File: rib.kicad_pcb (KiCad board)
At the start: 2 copper layers, 140 x 90 mm, 94 parts, among them J1 RJ45_LED, J10 Conn_01x04_Male, J11 Screw_Terminal_01x02, J12 Screw_Terminal_01x02, J13 Screw_Terminal_01x02, J14 Conn_01x02_Male, J15 Conn_01x02_Male, J16 Conn_01x06_Male, J2 RJ45_LED, J3 RJ45_LED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

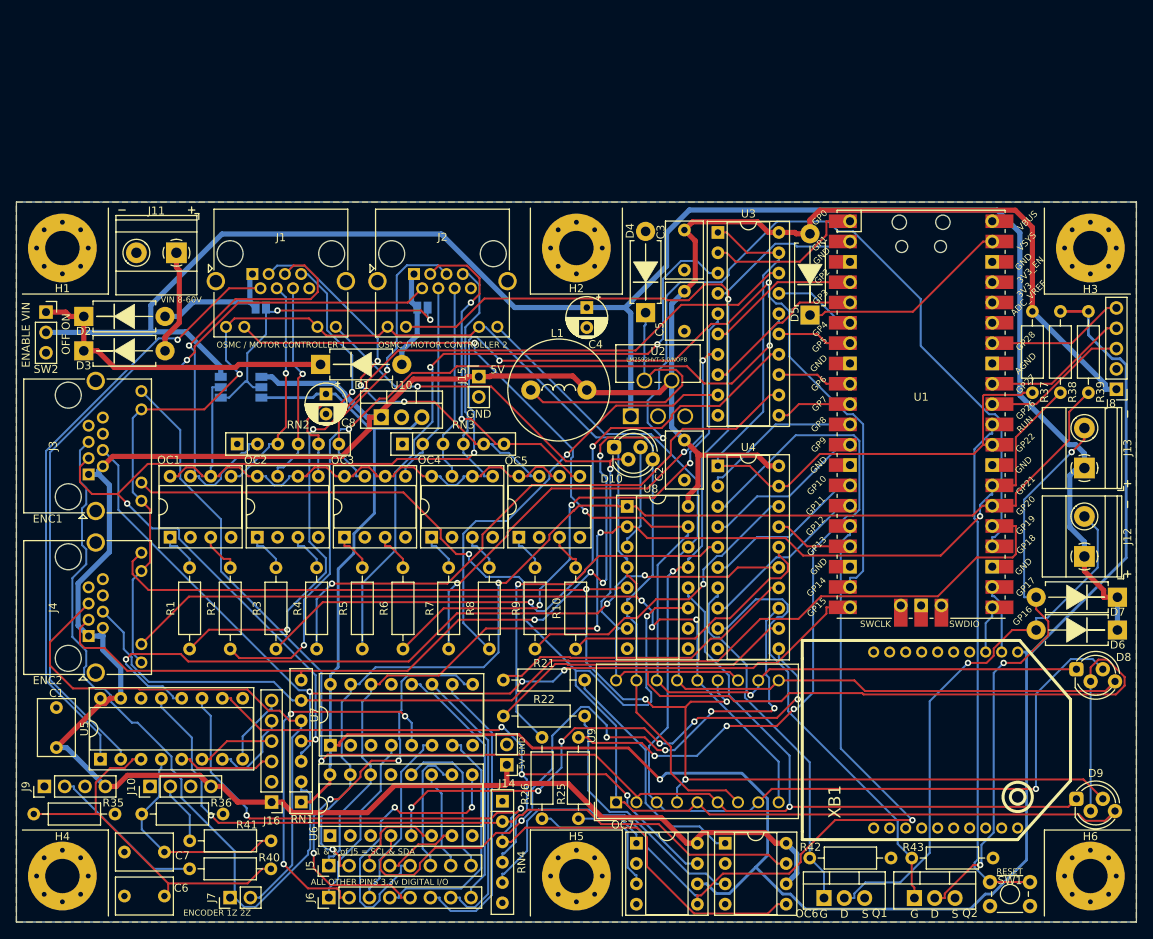
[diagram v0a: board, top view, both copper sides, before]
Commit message: Fix via stitching
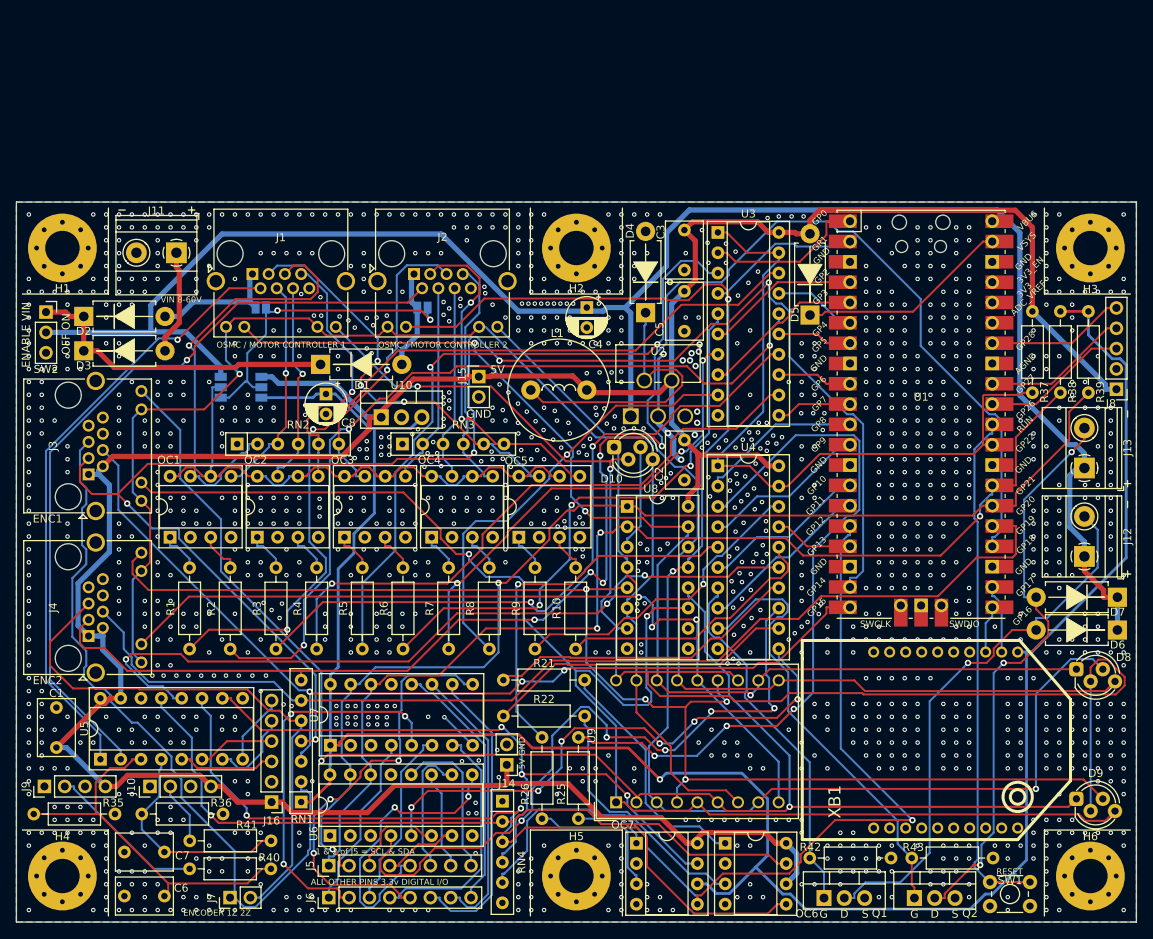
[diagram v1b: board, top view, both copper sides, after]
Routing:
- net GND: track 0.00 -> 19.8 mm, vias 0 -> 1422
- net Net-(RN1-R6): track 198.8 -> 200.0 mm
- net Net-(J5-Pin_5): track 37.6 -> 36.7 mm
- net LED8: track 122.2 -> 122.7 mm

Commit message: prepare to add zener diode
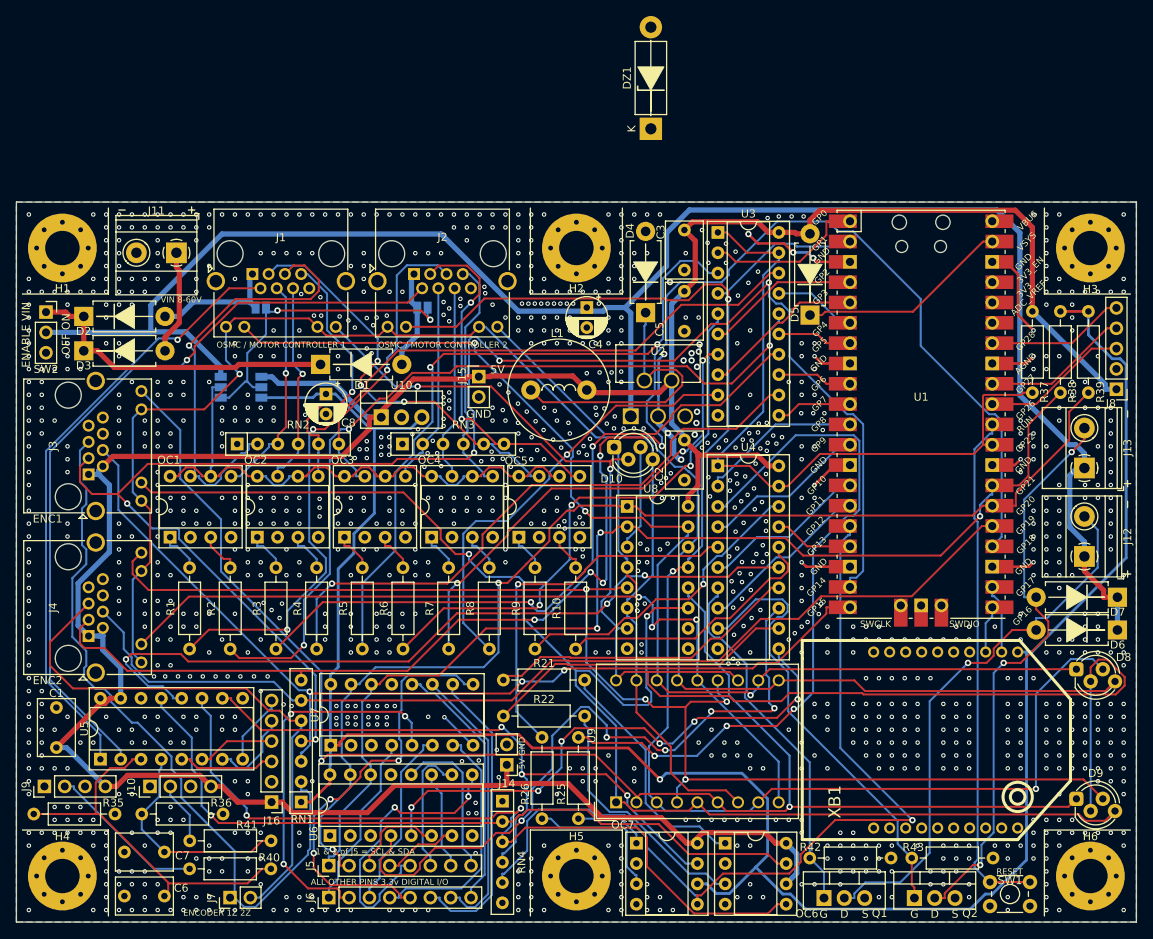
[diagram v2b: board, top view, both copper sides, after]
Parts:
- added DZ1: 1N5339B, Diode_THT_AKL:D_5W_CASE-017AA_P12.70mm_Horizontal_Zener, F.Cu at (114.8, 37.8)
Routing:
- net GND: track 19.8 -> 77.1 mm, vias 1422 -> 1221
- net Net-(RN1-R5): track 134.6 -> 126.7 mm

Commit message: v1.0 design update (BOMs not updated)
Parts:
- moved DZ1 24.9 mm to (114.1, 62.8)
- moved C4 16.5 mm to (93.7, 70.3)
- moved J15 6.06 mm to (87.5, 67.2), turned to 90 degrees
- moved D4 3.87 mm to (110.3, 60.9), turned to 180 degrees
- moved D10 0.14 mm to (110.2, 77.8)
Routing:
- net 5V: track 376.8 -> 479.7 mm, vias 0 -> 1
- net Net-(RN1-R2): track 123.4 -> 199.5 mm, vias 3 -> 7
- net GND: track 77.1 -> 2.54 mm, vias 1221 -> 2419
- net SDA: track 145.1 -> 215.3 mm, vias 2 -> 4
- net Net-(U1-GPIO16): track 5.93 -> 73.1 mm, vias 0 -> 5
- net Net-(J6-Pin_6): track 37.8 -> 92.1 mm, vias 0 -> 3
- net SCL: track 142.4 -> 190.8 mm, vias 3 -> 4
- net Net-(RN1-R3): track 202.4 -> 154.8 mm, vias 5 -> 3
- net Net-(RN3-R4): track 51.9 -> 97.4 mm, vias 3 -> 0
- net Net-(J6-Pin_7): track 35.1 -> 79.4 mm, vias 0 -> 3
- net Net-(U1-GPIO22): track 88.5 -> 126.2 mm
- net Net-(U3-1Y3): track 76.7 -> 113.7 mm
- net Net-(U4-2Y0): track 89.7 -> 59.9 mm, vias 3 -> 1
- net Net-(RN4-R4): track 110.8 -> 139.1 mm, vias 1 -> 5
- net Net-(U3-1Y2): track 88.1 -> 115.4 mm, vias 2 -> 1
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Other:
- board text added: "Designed by Amelia Deck for ILLINOIS TECH ROBOTICS Robot Interface Board (RIB) V1.0 inspired by GOLIATH design by Nash Kaminski with help from Scarlett Kadan Iliyan Jivraj"
- board text removed: "Designed by Amelia Deck for ILLINOIS TECH ROBOTICS Robot Interface Board (RIB) V1.0-RC1 inspired by GOLIATH design by Nash Kaminski with help from Scarlett Kadan Iliyan Jivraj"

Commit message: RIB v1.1 pre-release, documentation
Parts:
- removed R35, R36: 10k, Resistor_THT:R_Axial_DIN0207_L6.3mm_D2.5mm_P10.16mm_Horizontal
- added J17: Conn_01x02_Male, Connector_PinHeader_2.54mm:PinHeader_1x02_P2.54mm_Vertical, F.Cu at (65.5, 126.8)
- added J18: Conn_01x02_Male, Connector_PinHeader_2.54mm:PinHeader_1x02_P2.54mm_Vertical, F.Cu at (60.9, 126.7)
- added J19: Conn_01x02_Male, Connector_PinHeader_2.54mm:PinHeader_1x02_P2.54mm_Vertical, F.Cu at (54.6, 70.4)
- C6, C7: value 1uF -> 10uF
- J7: value Conn_01x02_Male -> Conn_01x04_Male; footprint Connector_PinHeader_2.54mm:PinHeader_1x02_P2.54mm_Vertical -> Connector_PinHeader_2.54mm:PinHeader_1x04_P2.54mm_Vertical
- R40, R41: value 33k -> 10k
- RN1: value 10k_Network06 -> R_Network08; footprint Resistor_THT:R_Array_SIP7 -> Resistor_THT:R_Array_SIP9
- moved R40 20.5 mm to (37.8, 123.4)
- moved R41 6.88 mm to (51.2, 123.4)
- moved RN1 5.12 mm to (71.1, 127.1)
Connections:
- J3 pad 3: Net-(RN1-R3) -> Net-(RN1-R5)
- J3 pad 4: Net-(RN1-R2) -> Net-(RN1-R4)
- J3 pad 6: GND -> Net-(J7-Pin_2)
- J4 pad 3: Net-(RN1-R6) -> Net-(RN1-R8)
- J4 pad 4: Net-(RN1-R5) -> Net-(RN1-R7)
- J4 pad 5: Net-(J7-Pin_2) -> Net-(J7-Pin_3)
- J4 pad 6: GND -> Net-(J7-Pin_4)
- RN1 pad 2: Net-(J7-Pin_1) -> Net-(J7-Pin_2)
- RN1 pad 3: Net-(RN1-R2) -> Net-(J7-Pin_4)
- RN1 pad 4: Net-(RN1-R3) -> Net-(J7-Pin_1)
- RN1 pad 5: Net-(J7-Pin_2) -> Net-(RN1-R4)
- RN1 pad 7: Net-(RN1-R6) -> Net-(J7-Pin_3)
- U1 pad 19: Net-(RN1-R3) -> Net-(RN1-R5)
- U1 pad 20: Net-(RN1-R2) -> Net-(RN1-R4)
- U1 pad 24: Net-(RN1-R6) -> Net-(RN1-R8)
- U1 pad 25: Net-(RN1-R5) -> Net-(RN1-R7)
- U6 pad 13: unconnected-(U6-~{INT}-Pad13) -> Net-(J17-Pin_2)
- U7 pad 13: unconnected-(U7-~{INT}-Pad13) -> Net-(J17-Pin_1)
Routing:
- net Net-(RN1-R4): track 0.00 -> 199.6 mm, vias 0 -> 7
- net Net-(RN1-R2): track 199.5 -> 0.00 mm, vias 7 -> 0
- net Net-(RN1-R8): track 0.00 -> 193.8 mm, vias 0 -> 9
- net Net-(RN1-R6): track 193.7 -> 0.00 mm, vias 9 -> 0
- net Net-(RN1-R3): track 154.8 -> 0.00 mm, vias 3 -> 0
- net Net-(RN1-R7): track 0.00 -> 149.8 mm, vias 0 -> 8
- net Net-(J7-Pin_4): track 0.00 -> 92.3 mm, vias 0 -> 4
- net Net-(J7-Pin_3): track 0.00 -> 72.8 mm, vias 0 -> 1
- net Net-(J17-Pin_1): track 0.00 -> 44.9 mm, vias 0 -> 4
- net 3.3V: track 265.4 -> 298.0 mm, vias 4 -> 6
- net Net-(J7-Pin_2): track 72.1 -> 103.7 mm, vias 0 -> 2
- net Net-(J17-Pin_2): track 0.00 -> 29.4 mm, vias 0 -> 2
- net Net-(J6-Pin_6): track 92.1 -> 64.2 mm
- net Net-(U5-CH2): track 46.7 -> 27.7 mm
- net Net-(J9-Pin_2): track 20.0 -> 5.37 mm
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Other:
- board text added: "Designed by Amelia Deck for ILLINOIS TECH ROBOTICS Robot Interface Board (RIB) V1.1 inspired by GOLIATH design by Nash Kaminski with help from Scarlett Kadan Iliyan Jivraj"
- board text removed: "Designed by Amelia Deck for ILLINOIS TECH ROBOTICS Robot Interface Board (RIB) V1.0 inspired by GOLIATH design by Nash Kaminski with help from Scarlett Kadan Iliyan Jivraj"
